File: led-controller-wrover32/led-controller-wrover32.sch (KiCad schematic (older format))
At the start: 55 parts, among them J1 Micro_SD_Card, J2 Conn_01x12, J3 USB_B_Micro, J4 Conn_01x12, J5 Conn_01x04 DNS, J6 Conn_01x02 DNS, J7 Conn_01x03 DNS, J8 Conn_01x05 DNS, J9 Conn_01x02 DNS, Q1 MMSS8050-H-TP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

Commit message: Fixed microphone, fan PWM and speaker
The ground was not hooked up to the microphone due to an issue with the
footprint.

The PWM pin was also used by the microphone.  Moved PWM pin to IO 5 which is
also shared with 5V output.

The speaker LR clock was using IO34 which is input only.  Moved to IO33 which
is also shared with a 5V output.

Updated revision to 3.0.1.
Fixed page settings, updated dates and revisions.

Signed-off-by: Aaron Williams <aaron.w2@gmail.com>
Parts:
- MIC1: footprint digikey-footprints:SPH0645LM4H-B -> Aaron:SPH0645LM4H-B
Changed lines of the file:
@@
 Sheet 1 4
 Title "Wrover32 LED Controller"
-Date "2019-05-23"
-Rev "2.1.0"
+Date "2019-11-15"
+Rev "3.0.1"
 Comp ""
 Comment1 "Copyright © 2019 by Aaron Williams"
@@
 FET_1A
 Text Label 650  2800 0    50   ~ 0
-IO26
+IO5
 Text Label 5500 7300 0    50   ~ 0
 IO0
@@
 F1 "Amplifier.sch" 50
 $EndSheet
-Text GLabel 3300 5550 0    50   Output ~ 0
-IO34
+Text GLabel 3300 5450 0    50   Output ~ 0
+IO33
 Text GLabel 3300 5050 0    50   Output ~ 0
 IO25
 Wire Wire Line
 	3750 5650 3550 5650
-Wire Wire Line
-	3750 5450 3550 5450
 Wire Wire Line
 	3550 5350 3750 5350
@@
 Wire Wire Line
 	3300 5150 3750 5150
-Wire Wire Line
-	3300 5550 3750 5550
 Wire Wire Line
 	3550 4550 3750 4550
@@
 F 0 "MIC1" H 2294 7453 60  0000 L CNN
 F 1 "SPH0645LM4H-B" H 2294 7347 60  0000 L CNN
-F 2 "digikey-footprints:SPH0645LM4H-B" H 2050 7600 60  0001 L CNN
+F 2 "Aaron:SPH0645LM4H-B" H 2050 7600 60  0001 L CNN
 F 3 "https://media.digikey.com/pdf/Data%20Sheets/Knowles%20Acoustics%20PDFs/SPH0645LM4H-B.pdf" H 2050 7700 60  0001 L CNN
 F 4 "423-1405-1-ND" H 2050 7800 60  0001 L CNN "Digi-Key_PN"
@@
 Wire Wire Line
 	9650 1950 10100 1950
+Wire Wire Line
+	3750 5550 3550 5550
+Wire Wire Line
+	3300 5450 3750 5450
 $EndSCHEMATC

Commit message: Minor cleanup
Signed-off-by: Aaron Williams <aaron.w2@gmail.com>
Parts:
- J2, J4: value Conn_01x12 -> BM12B-SRSS-TBT(LF)(SN)
- U2: value ESP32-WROVER-I -> ESP32-WROVER; MPN ESP32-WROVER-B (16MB) -> ESP32-WROVER (16MB); SPN 356-ESP32-WROB(16MB) -> 1904-1015-1-ND; SPR Mouser -> Digikey; SPURL - -> https://www.digikey.com/product-detail/en/espressif-systems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
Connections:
- net labels added: SCL, SDA
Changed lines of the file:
@@
 P 4350 4650
 F 0 "U2" H 3700 5900 50  0000 C CNN
-F 1 "ESP32-WROVER-I" H 4350 5926 50  0000 C CNN
+F 1 "ESP32-WROVER" H 4350 5926 50  0000 C CNN
 F 2 "ESP32:ESP32-WROOVER" H 4350 4650 50  0001 L BNN
 F 3 "https://www.espressif.com/sites/default/files/documentation/esp32-wrover-b_datasheet_en.pdf" H 4350 4650 50  0001 L BNN
 F 4 "Espressif Systems" H 0   0   50  0001 C CNN "MFR"
-F 5 "ESP32-WROVER-B (16MB)" H 0   0   50  0001 C CNN "MPN"
+F 5 "ESP32-WROVER (16MB)" H 0   0   50  0001 C CNN "MPN"
 F 6 "Espressif Systems" H 4350 4650 50  0001 L BNN "Field6"
 F 7 "Module Espressif Systems" H 4350 4650 50  0001 L BNN "Field7"
 F 8 "Module: combo; GPIO, I2C x2, I2S x2, SDIO, SPI x3, UART x3; U.FL" H 4350 4650 50  0001 L BNN "Field8"
-F 9 "Mouser" H 0   0   50  0001 C CNN "SPR"
-F 10 "356-ESP32-WROB(16MB)" H 0   0   50  0001 C CNN "SPN"
-F 11 "-" H 0   0   50  0001 C CNN "SPURL"
+F 9 "Digikey" H 0   0   50  0001 C CNN "SPR"
+F 10 "1904-1015-1-ND" H 0   0   50  0001 C CNN "SPN"
+F 11 "https://www.digikey.com/product-detail/en/espressif-systems/ESP32-WROVER-16MB/1904-1015-1-ND/9381724" H 0   0   50  0001 C CNN "SPURL"
 	1    4350 4650
 	1    0    0    -1
@@
 P 5250 7100
 F 0 "J4" H 5170 7817 50  0000 C CNN
-F 1 "Conn_01x12" H 5170 7726 50  0000 C CNN
+F 1 "BM12B-SRSS-TBT(LF)(SN)" V 5400 7100 50  0000 C CNN
 F 2 "Connectors_JST-BM12B-SURS-TF:BM12B-SRSS-TB" H 5250 7100 50  0001 C CNN
 F 3 "http://www.jst-mfg.com/product/pdf/eng/eSUR.pdf" H 5250 7100 50  0001 C CNN
@@
 P 3950 7100
 F 0 "J2" H 3870 7817 50  0000 C CNN
-F 1 "Conn_01x12" H 3950 7700 50  0000 C CNN
+F 1 "BM12B-SRSS-TBT(LF)(SN)" V 4100 7100 50  0000 C CNN
 F 2 "Connectors_JST-BM12B-SURS-TF:BM12B-SRSS-TB" H 3950 7100 50  0001 C CNN
 F 3 "http://www.jst-mfg.com/product/pdf/eng/eSUR.pdf" H 3950 7100 50  0001 C CNN
@@
 Wire Wire Line
 	3300 5450 3750 5450
+Text Label 7850 6150 0    50   ~ 0
+SDA
+Text Label 7850 6050 0    50   ~ 0
+SCL
 $EndSCHEMATC

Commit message: Cleanup
Signed-off-by: Aaron Williams <aaron.w2@gmail.com>
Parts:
- removed C7: 10uF, Capacitor_SMD:C_0805_2012Metric, symbol Device:C
- removed C8: 0.1uF, Capacitor_SMD:C_0603_1608Metric, symbol Device:C
- removed J7: Conn_01x03 DNS, Connector_PinHeader_1.27mm:PinHeader_1x03_P1.27mm_Vertical, symbol led-controller-wrover32-rescue:Conn_01x03-Connector-led-controller-wrover32-res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
- removed Q4: BSS214NW, TO_SOT_Packages_SMD:SOT-323_SC-70, symbol Transistor_FET:BSS214NW
- removed R11: 1m, Resistor_SMD:R_0603_1608Metric, symbol Device:R
- removed RN5: 22, Resistor_SMD:R_Array_Convex_4x0603, symbol Device:R_Pack04
- removed U4: MAX14611ETD+T, Maxim:TDFN--EP-14, symbol MAX14611ETD_T:MAX14611ETD+T
- added J7: Conn_01x02, Connector_PinHeader_1.27mm:PinHeader_1x02_P1.27mm_Vertical, symbol Connector_Generic:Conn_01x02
- added TP1: TestPoint, TestPoint:TestPoint_Pad_D1.0mm, symbol Connector:TestPoint
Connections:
- net labels added: IO0_RTS_DRV, IO2_RTS_DRV, RST_DTR_DRV, VBUS_REF
- net labels removed: FET_1A
- wire segments 253 -> 241
- no-connect marks 22 -> 20

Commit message: Fix reset circuit and other stuff
This fixes the reset circuit and moves a few components.  It also
cleans up the BOM a bit.

Also bumped to version 3.5.0

Signed-off-by: Aaron Williams <aaron.w2@gmail.com>
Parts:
- removed Q2: BC857BS, Package_TO_SOT_SMD:SOT-363_SC-70-6, symbol Transistor_BJT:BC857BS
- added Q2: FMB2222A, Package_TO_SOT_SMD:SOT-23-6, symbol Aaron:FMB2222A
- added TP2: DNI, TestPoint:TestPoint_Pad_D1.0mm, symbol Connector:TestPoint
- FID1, FID2, FID3, FID4: value FIDUCIAL_1MM -> DNI
- J5: value Conn_01x04 DNS -> Conn_01x04
- J6: value Conn_01x02 DNS -> Conn_01x02 DNI; MFR - -> Samtec Inc.; MPN - -> TMS-102-01-G-S; SPN - -> SAM12199-ND; SPR - -> Digikey; SPURL - -> https://www.digikey.com/products/en/connectors-interconnect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
- J7: value Conn_01x02 -> Conn_01x02 DNI; MFR (none) -> Samtec Inc.; MPN (none) -> TMS-102-01-G-S; SPN (none) -> SAM12199-ND; SPR (none) -> Digikey; SPURL (none) -> https://www.digikey.com/products/en/connectors-interconnect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
- J8: value Conn_01x05 DNS -> Conn_01x05 DNI; MFR - -> Samtec Inc.; MPN - -> TMS-105-01-G-S; SPN - -> SAM10245-ND; SPR - -> Digikey; SPURL - -> https://www.digikey.com/products/en/connectors-interconnect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
- J9: value Conn_01x02 DNS -> Conn_01x02 DNI
- R12: value 22.1k -> 22.1K
- R13: value 47.5k -> 47.5K
- R5, R6: value 10K -> 4.7K; MFR Vishay Dale -> Bourns Inc.; MPN CRCW060310K0FKEC -> CR0603-FX-4701ELF; SPN 541-2979-1-ND -> CR0603-FX-4701ELFCT-ND; SPURL - -> https://www.digikey.com/product-detail/en/bourns-inc/CR0603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
- RN3: value 10K -> 4.7K; MFR Panasonic -> Bourns Inc.; MPN EXB-V8V103JV -> CAT16-4701F4LF; SPN Y4103CT-ND -> CAT16-4701F4LFCT-ND; SPURL - -> https://www.digikey.com/product-detail/en/bourns-inc/CAT16-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
- TP1: value TestPoint -> DNI; MFR (none) -> -; MPN (none) -> -; SPN (none) -> -; SPR (none) -> -; SPURL (none) -> -
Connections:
- wire segments 241 -> 243
- no-connect marks 20 -> 18
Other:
- note removed: "J7 pin 3 can be used for PWM.\nNote that Wrover32 IO26\ncan do analog output."
- moved on the sheet: C14, J7

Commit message: Moved WS2813B after fixing footprint  v3.6
Signed-off-by: Aaron Williams <aaron.w2@gmail.com>
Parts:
- C16, C17: MFR AVX -> Murata Electronics; MPN 06035C104K4Z4A -> GCM188R71H104KA57D; SPN 478-10679-1-ND -> 490-4779-1-ND; SPURL https://www.digikey.com/product-detail/en/avx-corporation/0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 -> https://www.digikey.com/product-detail/en/murata-electronic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
- D1: MPN WS2813-Mini -> WS2813B-Mini
- FID1, FID2, FID3, FID4, TP1, TP2: value DNI -> DNF
- J6, J7, J9: value Conn_01x02 DNI -> Conn_01x02 DNF
- J8: value Conn_01x05 DNI -> Conn_01x05 DNF
- RN4: MPN EXB-V8V103JV -> EXB-18V104JX; SPN Y4103CT-ND -> Y6104CT-ND; SPURL - -> https://www.digikey.com/product-detail/en/panasonic-electro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

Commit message: Changed UART to CP2104 to simplify.
Signed-off-by: Aaron Williams <aaron.w2@gmail.com>
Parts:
- removed R12: 22.1K, Resistor_SMD:R_0603_1608Metric, symbol led-controller-wrover32-rescue:R-device-led-controller-wrover32-rescue
- removed R13: 47.5K, Resistor_SMD:R_0603_1608Metric, symbol led-controller-wrover32-rescue:R-device-led-controller-wrover32-rescue
- removed U3: CP2102N-A01-GQFN24, Aaron:QFN-24-1EP_4x4mm_Pitch0.5mm_rounded_corners, symbol Interface_USB:CP2102N-A01-GQFN24
- added U3: CP2104, Package_DFN_QFN:QFN-24-1EP_4x4mm_P0.5mm_EP2.6x2.6mm, symbol Interface_USB:CP2104
- RN4: MPN EXB-18V104JX -> EXB-V8V104JV; SPN Y6104CT-ND -> Y4104CT-ND; SPURL https://www.digikey.com/product-detail/en/panasonic-electronic-components/EXB-18V104JX/Y6104CT-ND/671426 -> https://www.digikey.com/product-detail/en/panasonic-electronic-components/EXB-V8V104JV/Y4104CT-ND/155183
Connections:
- net labels removed: VBUS_REF
- wire segments 243 -> 239
- no-connect marks 18 -> 20
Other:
- moved on the sheet: C6, TP2

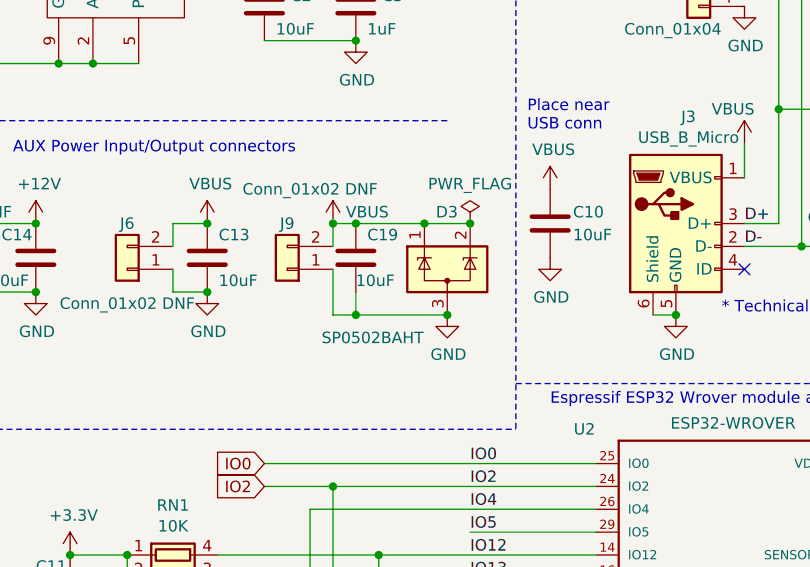
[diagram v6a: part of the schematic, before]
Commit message: Minor changes
- Tweaked some of the component values in the 12V supply as per TI.
- Removed unnecessary protection diode, the USB one is enough.
- Changed UART to CS2104 which eliminates two resistors and is
  slightly cheaper
- Updated PCB to reflect changes.

Signed-off-by: Aaron Williams <aaron.w2@gmail.com>
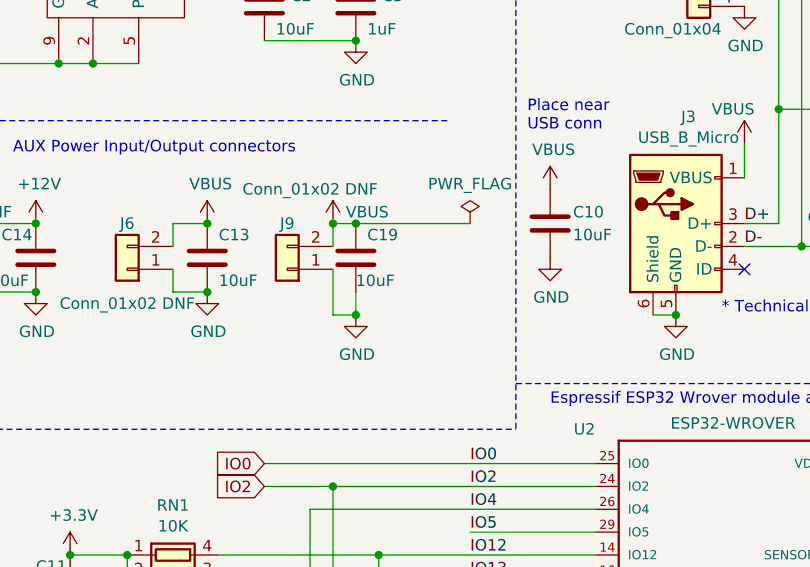
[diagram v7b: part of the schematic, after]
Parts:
- removed D3: SP0502BAHT, Package_TO_SOT_SMD:SOT-23, symbol Power_Protection:SP0502BAHT
- C1, C10, C13, C14, C18, C19, C2, C4, C6, C9: DESC (none) -> CAP CER 10UF 16V X7R 0805
- C11, C15, C3: DESC (none) -> CAP CER 1UF 10V X7R 0603
- C12: DESC (none) -> CAP CER 22UF 10V X5R 0805
- C16, C17: DESC (none) -> CAP CER 0.1UF 50V X7R 0603
- D1: DESC (none) -> RGB 620~625nm Red, 515~525nm Green, 465~475nm Blue SMD-6 Li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
- D2: DESC (none) -> TVS DIODE 5.25V 17V SOT666
- FID1, FID2, FID3, FID4, J9, TP1, TP2: DESC (none) -> -
- J1: DESC (none) -> CONN MICRO SD CARD HINGED TYPE
- J2, J4: DESC (none) -> CONN HEADER SMD 12POS 1MM
- J3: DESC (none) -> CONN RCPT USB2.0 MICRO B SMD R/A
- J5: DESC (none) -> CONN HEADER VERT 4POS 2MM
- J6, J7: DESC (none) -> CONN HEADER VERT 2POS 1.27MM
- J8: DESC (none) -> CONN HEADER VERT 5POS 1.27MM
- MIC1: DESC (none) -> CRAWFORD MIC DGT I2S BOTTOM PORT
- Q1: DESC (none) -> TRANS NPN 25V 1.5A SOT23
- Q2: DESC (none) -> TRANS 2NPN 40V 0.5A 6SSOT
- Q3: DESC (none) -> N-Channel 50V 220mA (Ta) 360mW (Ta) Surface Mount SOT-23-3
- R1: DESC (none) -> RES SMD 10K OHM 1% 1/10W 0603
- R10: DESC (none) -> RES SMD 100K OHM 5% 1/10W 0603
- R5, R6: DESC (none) -> RES SMD 4.7K OHM 1% 1/10W 0603
- RN1: DESC (none) -> 10k Ohm +/- 5% Isolated Resistor Network, 0606, Concave
- RN2: DESC (none) -> RES ARRAY 4 RES 10K OHM 1206
- RN3: DESC (none) -> RES ARRAY 4 RES 4.7K OHM 1206
- RN4: DESC (none) -> RES ARRAY 4 RES 100K OHM 1206
- U1: DESC (none) -> DC DC CONVERTER 3.3V
- U2: DESC (none) -> WIFI MODULE 128MBITS SPI FLASH
- U3: DESC (none) -> IC SGL USB-TO-UART BRIDGE 24QFN; MFR (none) -> Silicon Labs; MPN (none) -> CP2104-F03-GMR; SPN (none) -> 336-4146-1-ND; SPR (none) -> Digikey; SPURL (none) -> https://www.digikey.com/products/en/integrated-circuits-ics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
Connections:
- wire segments 239 -> 237

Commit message: Multiple changes from v3.7
1. Fixed microphone so it uses the left channel
2. Reduced the number of unique components, i.e. replacing a couple of
   resistor networks with already used resistors
3. Removed unneeded resistor in programming circuit
4. Moved speaker chip to the other side to be closer to the connector
5. Cleaned up some of the traces and removed some inner-layer traces.
6. Moved reset switch to the edge to make access easier.
7. Added big via to line up with daughter card.
8. Replaced BSS138 transistor array with two BSS138 transistors to reduce
   the unique component count and reduce cost.

Signed-off-by: Aaron Williams <aaron.w2@gmail.com>
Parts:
- removed RN1: 10K, Resistor_SMD:R_Array_Convex_2x0603, symbol Device:R_Pack02
- removed RN3: 4.7K, Resistor_SMD:R_Array_Convex_4x0603, symbol Device:R_Pack04
- removed TP1: DNF, TestPoint:TestPoint_Pad_D1.0mm, symbol Connector:TestPoint
- added R11, R3, R9: 10K, Resistor_SMD:R_0603_1608Metric, symbol Device:R
- added R4, R7, R8: 4.7K, Resistor_SMD:R_0603_1608Metric, symbol Device:R
- C1, C10, C13, C14, C18, C19, C2, C4, C6, C9: SPURL - -> https://www.digikey.com/products/en?keywords=1276-2872-1-ND
- C11, C15, C3: SPURL - -> https://www.digikey.com/products/en?keywords=1276-1946-1-ND
- D2: SPURL - -> https://www.digikey.com/products/en?keywords=497-5026-1-ND
- J3: SPURL - -> https://www.digikey.com/products/en?keywords=WM1399CT-ND
- J5: SPURL - -> https://www.digikey.com/products/en?keywords=455-1706-ND
- Q2: SPURL - -> https://www.digikey.com/products/en?keywords=FMB2222ACT-ND
- Q2: SPURL https://www.digikey.com/product-detail/en/on-semiconductor/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 -> https://www.digikey.com/products/en?keywords=FMB2222ACT-ND
- Q3: SPURL - -> https://www.digikey.com/product-detail/en/on-semiconductor/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
- R1: SPURL - -> https://www.digikey.com/products/en?keywords=541-2979-1-ND
- R10: value 100K -> 86.6K; DESC RES SMD 100K OHM 5% 1/10W 0603 -> RES SMD 86.6K OHM 1% 1/10W 0603; MPN CRCW0603100KJNEA -> CRCW060386K6FKEA; SPN 541-100KGCT-ND -> 541-86.6KHCT-ND; SPURL - -> https://www.digikey.com/products/en?keywords=541-86.6KHCT-ND
- RN2: SPURL - -> https://www.digikey.com/products/en?keywords=Y4103CT-ND
- U1: symbol Torex_Semiconductor:XCL21X -> led-controller-wrover32-rescue:XCL21X-Torex_Semiconductor; SPURL - -> https://www.digikey.com/products/en?keywords=893-1279-1-ND
- U2: value ESP32-WROVER -> ESP32-WROVER-B; MPN ESP32-WROVER (16MB) -> ESP32-WROVER (16MB) ESP32-WROVER-B
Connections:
- net labels added: ~INT
- wire segments 237 -> 236
